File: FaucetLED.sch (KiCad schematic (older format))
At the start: 25 parts, among them P1 CONN_01X13, P2 CONN_01X02, U1 MAX4256

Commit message: WIP version 2 with STM32L0.
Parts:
- removed D1: LED_RCBG, Pin_Headers:Pin_Header_Straight_1x04, symbol LED_RCBG
- removed P1: CONN_01X13, Socket_Strips:Socket_Strip_Straight_1x13, symbol CONN_01X13
- removed P2: CONN_01X02, Pin_Headers:Pin_Header_Straight_1x02, symbol CONN_01X02
- removed R10: 68R, Resistors_ThroughHole:Resistor_Horizontal_RM10mm, symbol R
- removed R11, R12: 10R, Resistors_ThroughHole:Resistor_Horizontal_RM10mm, symbol R
- removed R3, R5: 100M, Resistors_ThroughHole:Resistor_Horizontal_RM10mm, symbol R
- removed R6: 680R, Resistors_ThroughHole:Resistor_Horizontal_RM10mm, symbol R
- removed TH1: THERMISTOR, Pin_Headers:Pin_Header_Straight_1x02, symbol THERMISTOR
- removed U1: MAX4256, Housings_SOIC:SOIC-8_3.9x4.9mm_Pitch1.27mm, symbol MAX4256
- added BT2: LiIon, Pin_Headers:Pin_Header_Angled_1x02_Pitch2.00mm, symbol Battery
- added C3: 0.1u, Capacitors_SMD:C_0603, symbol C
- added D1: LED, LEDs:LED_0805, symbol LED
- added L1: Bead, Resistors_SMD:R_0603, symbol L_Small
- added P1: CONN_01X07, Pin_Headers:Pin_Header_Straight_1x07_Pitch2.54mm, symbol CONN_01X07
- added P2: CONN_01X03, Pin_Headers:Pin_Header_Straight_1x03_Pitch2.54mm, symbol CONN_01X03
- added R1: 100R, Resistors_SMD:R_0603, symbol R
- added R4: 10k, Resistors_SMD:R_0603, symbol R
- added R9: 1k, Resistors_SMD:R_0603, symbol R
- added U1: TLV70033DDC, TO_SOT_Packages_SMD:SOT-23-5, symbol TLV70033DDC
- added U2: STM32L052KxTx, Housings_QFP:LQFP-32_7x7mm_Pitch0.8mm, symbol STM32L052KxTx
- added W1: TEST_1P, Measurement_Points:Measurement_Point_Round-SMD-Pad_Small, symbol TEST_1P
- BT1: value Battery -> CR2016x2; footprint Pin_Headers:Pin_Header_Straight_1x02 -> Connect:CR2032H
- C1: value 10n -> 0.1u; footprint Capacitors_ThroughHole:C_Rect_L7_W2_P5 -> Capacitors_SMD:C_0603
- C2: value 10p -> 1u; footprint Capacitors_ThroughHole:C_Rect_L7_W2_P5 -> Capacitors_SMD:C_0603
- C4: value 10p -> 0.47u; footprint Capacitors_ThroughHole:C_Rect_L7_W2_P5 -> Capacitors_SMD:C_0603
- C6: value 0.1u -> 1u; footprint Capacitors_ThroughHole:C_Rect_L7_W2_P5 -> Capacitors_SMD:C_0603
- C7: renamed from C3; value 1u -> 0.1u; footprint Capacitors_ThroughHole:C_Rect_L7_W2_P5 -> Capacitors_SMD:C_0603
- C8: renamed from C5; footprint Capacitors_ThroughHole:C_Rect_L7_W2_P5 -> Capacitors_SMD:C_0603
- C9: renamed from C7; footprint Capacitors_ThroughHole:C_Rect_L7_W2_P5 -> Capacitors_SMD:C_0603
- R2: renamed from R1; footprint Resistors_ThroughHole:Resistor_Horizontal_RM10mm -> Resistors_SMD:R_0603
- R3: renamed from R2; footprint Resistors_ThroughHole:Resistor_Horizontal_RM10mm -> Resistors_SMD:R_0603
- R5: renamed from R4; footprint Resistors_ThroughHole:Resistor_Horizontal_RM10mm -> Resistors_SMD:R_0603
- R6: renamed from R7; value 68R -> 78R; footprint Resistors_ThroughHole:Resistor_Horizontal_RM10mm -> Resistors_SMD:R_0603
- R7: renamed from R8; value 15R -> 12R; footprint Resistors_ThroughHole:Resistor_Horizontal_RM10mm -> Resistors_SMD:R_0603
- R8: renamed from R9; value 15R -> 25R; footprint Resistors_ThroughHole:Resistor_Horizontal_RM10mm -> Resistors_SMD:R_0603
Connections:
- net labels added: BATT_2, LED_B_OUT, LED_DBG, LED_G_OUT, LED_R_OUT, MCO, RESET, SWCLK, SWDIO, THERM_SENSE, THERM_SW, TSC_IN, TSC_SAMPLING
- net labels removed: AMP_SHDN, PIEZO_1, PIEZO_2, PIEZO_AMP, THERM_1, THERM_2, T_SENSE, VCC_2, VCC_2_BUF
- wire segments 84 -> 79
- no-connect marks 4 -> 13
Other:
- moved on the sheet: BT1, C7, C8, C9, R2, R3, R5, R6, R7, R8

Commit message: Add battery holder, more connectors.
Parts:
- removed P1: CONN_01X07, Pin_Headers:Pin_Header_Straight_1x07_Pitch2.54mm, symbol CONN_01X07
- added D1: D_Schottky_x2_KCom_AAK, TO_SOT_Packages_SMD:SOT-23, symbol D_Schottky_x2_KCom_AAK
- added P1: CONN_01X03, Pin_Headers:Pin_Header_Straight_1x03_Pitch2.54mm, symbol CONN_01X03
- added P2, P3, P5: CONN_01X02, Pin_Headers:Pin_Header_Straight_2x01_Pitch2.54mm, symbol CONN_01X02
- BT1: footprint Connect:CR2032H -> components:Keystone_3020_CR2016x2
- U1: DigiKey PN (none) -> 296-27937-1-ND
- renumbered C6 to C5, C7 to C6, C8 to C7, C9 to C8, D1 to D2, P2 to P4
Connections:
- wire segments 79 -> 86
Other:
- moved on the sheet: BT1, C1, C2, C5, P4, U1

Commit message: Add part numbers for more parts.
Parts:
- BT1: DigiKey PN (none) -> 36-3020-ND; Manufacturer PN (none) -> 3020
- D2: DigiKey PN (none) -> 67-2191-1-ND
- L1: Manufacturer PN (none) -> BK1608HW601-T
- U1: Manufacturer PN (none) -> TLV70033DDCR
- U2: DigiKey PN (none) -> 497-14904-ND; Manufacturer PN (none) -> STM32L052K8T6
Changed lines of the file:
@@
 F 2 "components:Keystone_3020_CR2016x2" V 1400 1440 50  0001 C CNN
 F 3 "" V 1400 1440 50  0000 C CNN
+F 4 "36-3020-ND" H 1400 1400 60  0001 C CNN "DigiKey PN"
+F 5 "3020" H 1400 1400 60  0001 C CNN "Manufacturer PN"
 	1    1400 1400
 	1    0    0    -1
@@
 F 2 "Housings_QFP:LQFP-32_7x7mm_Pitch0.8mm" H 5500 2250 60  0001 C CNN
 F 3 "" H 5500 2250 60  0001 C CNN
+F 4 "497-14904-ND" H 5600 3100 60  0001 C CNN "DigiKey PN"
+F 5 "STM32L052K8T6" H 5600 3100 60  0001 C CNN "Manufacturer PN"
 	1    5600 3100
 	1    0    0    -1
@@
 F 3 "" H 4500 1150 50  0000 C CNN
 F 4 "296-27937-1-ND" H 4500 1150 60  0001 C CNN "DigiKey PN"
+F 5 "TLV70033DDCR" H 4500 1150 60  0001 C CNN "Manufacturer PN"
 	1    4500 1150
 	1    0    0    -1
@@
 F 2 "LEDs:LED_0805" H 8850 3250 50  0001 C CNN
 F 3 "" H 8850 3250 50  0000 C CNN
+F 4 "67-2191-1-ND" H 8850 3250 60  0001 C CNN "DigiKey PN"
 	1    8850 3250
 	-1   0    0    1
@@
 F 3 "" H 5800 2050 50  0000 C CNN
 F 4 "587-1879-1-ND" H 5800 2050 60  0001 C CNN "DigiKey PN"
+F 5 "BK1608HW601-T" H 5800 2050 60  0001 C CNN "Manufacturer PN"
 	1    5800 2050
 	1    0    0    -1

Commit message: Update R and C footprints for 0603/0805 compatibility.
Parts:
- C1, C2, C3, C4, C5, C6, C7, C8: footprint Capacitors_SMD:C_0603 -> components:C_0603_0805
- R1, R2, R3, R4, R5, R6, R7, R8, R9: footprint Resistors_SMD:R_0603 -> components:R_0603_0805
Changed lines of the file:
@@
 F 0 "R5" V 5480 5950 50  0000 C CNN
 F 1 "10k" V 5400 5950 50  0000 C CNN
-F 2 "Resistors_SMD:R_0603" V 5330 5950 50  0001 C CNN
+F 2 "components:R_0603_0805" V 5330 5950 50  0001 C CNN
 F 3 "" H 5400 5950 50  0000 C CNN
 	1    5400 5950
@@
 F 0 "R2" V 4030 5950 50  0000 C CNN
 F 1 "1M" V 3950 5950 50  0000 C CNN
-F 2 "Resistors_SMD:R_0603" V 3880 5950 50  0001 C CNN
+F 2 "components:R_0603_0805" V 3880 5950 50  0001 C CNN
 F 3 "" H 3950 5950 50  0000 C CNN
 	1    3950 5950
@@
 F 0 "R3" V 4030 6450 50  0000 C CNN
 F 1 "1M" V 3950 6450 50  0000 C CNN
-F 2 "Resistors_SMD:R_0603" V 3880 6450 50  0001 C CNN
+F 2 "components:R_0603_0805" V 3880 6450 50  0001 C CNN
 F 3 "" H 3950 6450 50  0000 C CNN
 	1    3950 6450
@@
 F 0 "C7" H 6375 1700 50  0000 L CNN
 F 1 "0.1u" H 6375 1500 50  0000 L CNN
-F 2 "Capacitors_SMD:C_0603" H 6388 1450 50  0001 C CNN
+F 2 "components:C_0603_0805" H 6388 1450 50  0001 C CNN
 F 3 "" H 6350 1600 50  0000 C CNN
 	1    6350 1600
@@
 F 0 "C8" H 6775 1700 50  0000 L CNN
 F 1 "1u" H 6775 1500 50  0000 L CNN
-F 2 "Capacitors_SMD:C_0603" H 6788 1450 50  0001 C CNN
+F 2 "components:C_0603_0805" H 6788 1450 50  0001 C CNN
 F 3 "" H 6750 1600 50  0000 C CNN
 	1    6750 1600
@@
 F 0 "C6" H 5425 6550 50  0000 L CNN
 F 1 "0.1u" H 5425 6350 50  0000 L CNN
-F 2 "Capacitors_SMD:C_0603" H 5438 6300 50  0001 C CNN
+F 2 "components:C_0603_0805" H 5438 6300 50  0001 C CNN
 F 3 "" H 5400 6450 50  0000 C CNN
 	1    5400 6450
@@
 F 0 "R7" V 8480 4700 50  0000 C CNN
 F 1 "12R" V 8400 4700 50  0000 C CNN
-F 2 "Resistors_SMD:R_0603" V 8330 4700 50  0001 C CNN
+F 2 "components:R_0603_0805" V 8330 4700 50  0001 C CNN
 F 3 "" H 8400 4700 50  0000 C CNN
 	1    8400 4700
@@
 F 0 "R8" V 8480 4900 50  0000 C CNN
 F 1 "25R" V 8400 4900 50  0000 C CNN
-F 2 "Resistors_SMD:R_0603" V 8330 4900 50  0001 C CNN
+F 2 "components:R_0603_0805" V 8330 4900 50  0001 C CNN
 F 3 "" H 8400 4900 50  0000 C CNN
 	1    8400 4900
@@
 F 0 "R6" V 8480 4500 50  0000 C CNN
 F 1 "78R" V 8400 4500 50  0000 C CNN
-F 2 "Resistors_SMD:R_0603" V 8330 4500 50  0001 C CNN
+F 2 "components:R_0603_0805" V 8330 4500 50  0001 C CNN
 F 3 "" H 8400 4500 50  0000 C CNN
 	1    8400 4500
@@
 F 0 "C4" H 4075 4300 50  0000 L CNN
 F 1 "0.47u" H 4075 4100 50  0000 L CNN
-F 2 "Capacitors_SMD:C_0603" H 4088 4050 50  0001 C CNN
+F 2 "components:C_0603_0805" H 4088 4050 50  0001 C CNN
 F 3 "" H 4050 4200 50  0000 C CNN
 	1    4050 4200
@@
 F 0 "R4" V 4630 3150 50  0000 C CNN
 F 1 "10k" V 4550 3150 50  0000 C CNN
-F 2 "Resistors_SMD:R_0603" V 4480 3150 50  0001 C CNN
+F 2 "components:R_0603_0805" V 4480 3150 50  0001 C CNN
 F 3 "" H 4550 3150 50  0000 C CNN
 	1    4550 3150
@@
 F 0 "C3" H 3975 3200 50  0000 L CNN
 F 1 "0.1u" H 3975 3000 50  0000 L CNN
-F 2 "Capacitors_SMD:C_0603" H 3988 2950 50  0001 C CNN
+F 2 "components:C_0603_0805" H 3988 2950 50  0001 C CNN
 F 3 "" H 3950 3100 50  0000 C CNN
 	1    3950 3100
@@
 F 0 "C5" H 5225 1400 50  0000 L CNN
 F 1 "1u" H 5225 1200 50  0000 L CNN
-F 2 "Capacitors_SMD:C_0603" H 5238 1150 50  0001 C CNN
+F 2 "components:C_0603_0805" H 5238 1150 50  0001 C CNN
 F 3 "" H 5200 1300 50  0000 C CNN
 	1    5200 1300
@@
 F 0 "C2" H 3775 1400 50  0000 L CNN
 F 1 "1u" H 3775 1200 50  0000 L CNN
-F 2 "Capacitors_SMD:C_0603" H 3788 1150 50  0001 C CNN
+F 2 "components:C_0603_0805" H 3788 1150 50  0001 C CNN
 F 3 "" H 3750 1300 50  0000 C CNN
 	1    3750 1300
@@
 F 0 "C1" H 3525 1400 50  0000 L CNN
 F 1 "0.1u" H 3525 1200 50  0000 L CNN
-F 2 "Capacitors_SMD:C_0603" H 3538 1150 50  0001 C CNN
+F 2 "components:C_0603_0805" H 3538 1150 50  0001 C CNN
 F 3 "" H 3500 1300 50  0000 C CNN
 	1    3500 1300
@@
 F 0 "R9" V 8530 3250 50  0000 C CNN
 F 1 "1k" V 8450 3250 50  0000 C CNN
-F 2 "Resistors_SMD:R_0603" V 8380 3250 50  0001 C CNN
+F 2 "components:R_0603_0805" V 8380 3250 50  0001 C CNN
 F 3 "" H 8450 3250 50  0000 C CNN
 	1    8450 3250
@@
 F 0 "R1" V 3830 4000 50  0000 C CNN
 F 1 "100R" V 3750 4000 50  0000 C CNN
-F 2 "Resistors_SMD:R_0603" V 3680 4000 50  0001 C CNN
+F 2 "components:R_0603_0805" V 3680 4000 50  0001 C CNN
 F 3 "" H 3750 4000 50  0000 C CNN
 	1    3750 4000

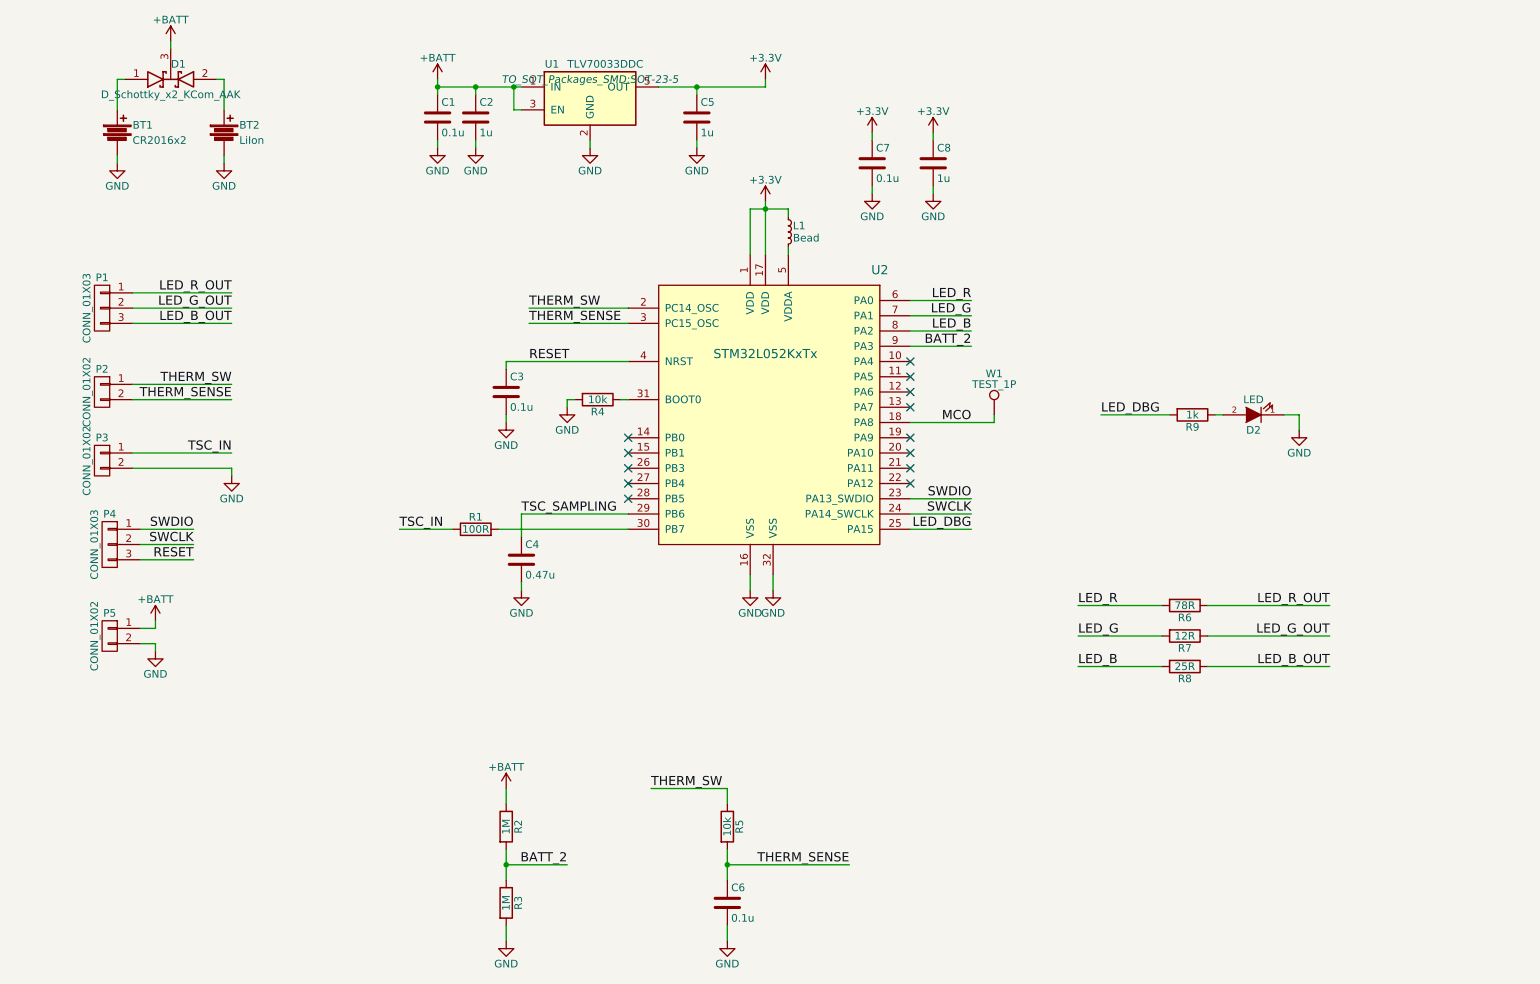
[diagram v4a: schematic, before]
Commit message: Add 5V regulator, LED drive NMOS. Not layed out in PCB yet.
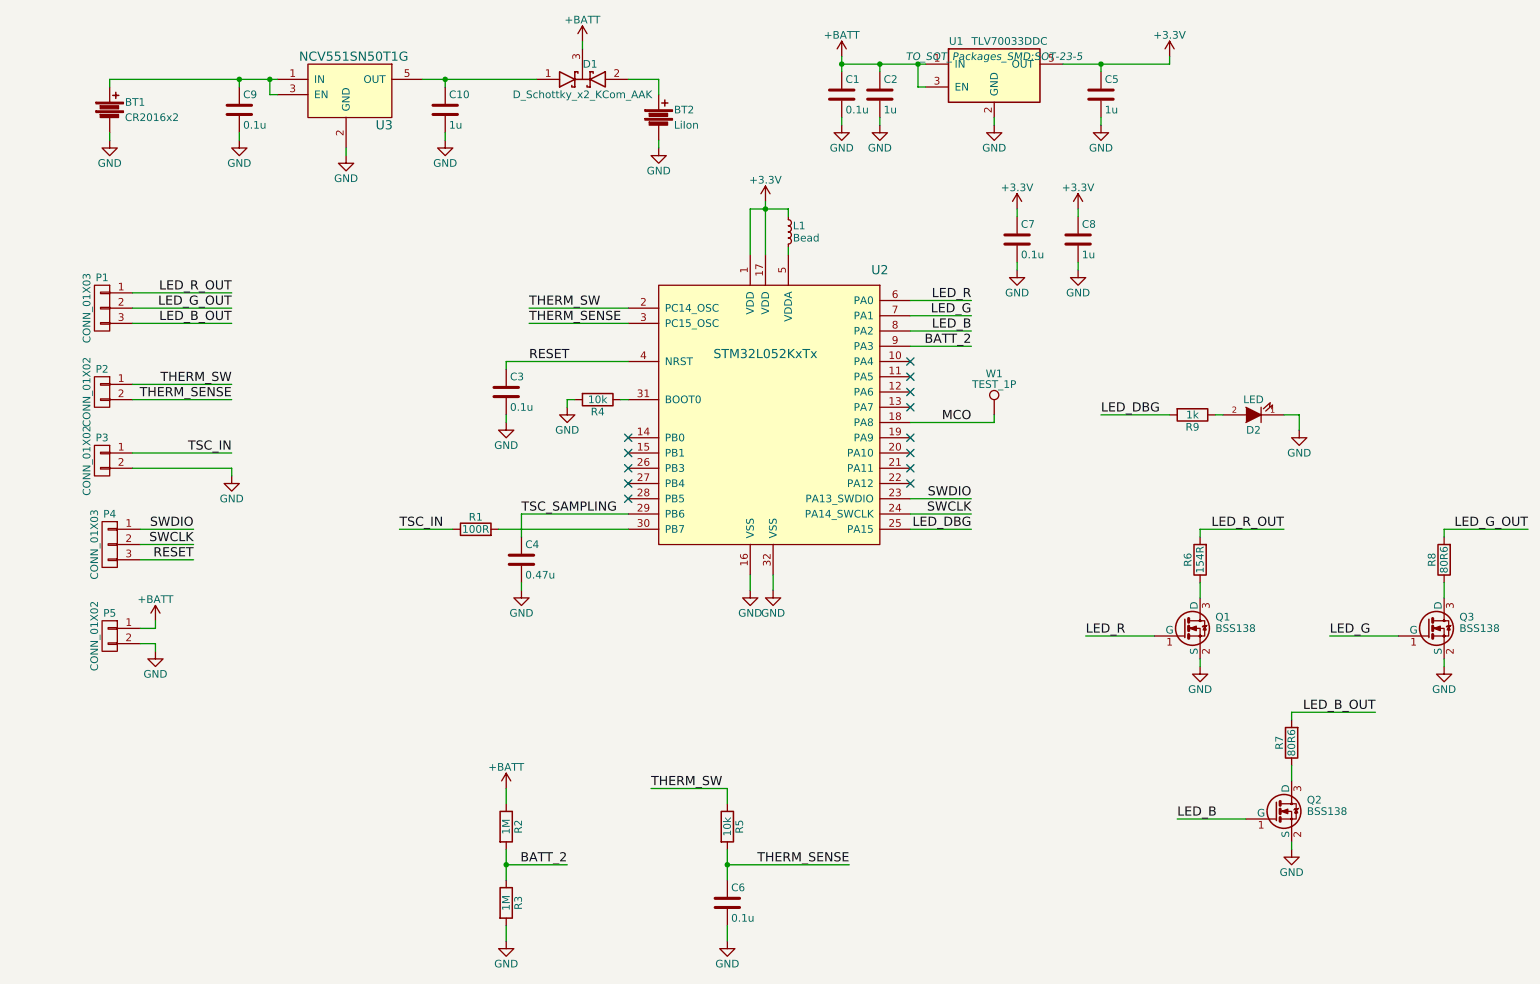
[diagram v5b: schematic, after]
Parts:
- added C10: 1u, components:C_0603_0805, symbol C
- added C9: 0.1u, components:C_0603_0805, symbol C
- added Q1, Q2, Q3: BSS138, TO_SOT_Packages_SMD:SOT-23, symbol BSS138
- added U3: NCV551SN50T1G, TO_SOT_Packages_SMD:SOT-23-5, symbol NCV551SN50T1G
- R6: value 78R -> 154R
- R7: value 12R -> 80R6
- R8: value 25R -> 80R6
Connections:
- net GND: now also C10.2, C9.2, Q1.2 (S), Q2.2 (S), Q3.2 (S), U3.2 (GND)
- net LED_B: now also Q2.1 (G); no longer R8.2
- net LED_B_OUT: now also R7.2; no longer R8.1
- net LED_G: now also Q3.1 (G); no longer R7.2
- net LED_G_OUT: now also R8.2; no longer R7.1
- net LED_R: now also Q1.1 (G); no longer R6.2
- net LED_R_OUT: now also R6.2; no longer R6.1
- net at BT1.1: now also C9.1, U3.1 (IN), U3.3 (EN); no longer D1.1 (A)
- new net: Q1.3 (D), R6.1
- new net: C10.1, D1.1 (A), U3.5 (OUT)
- new net: Q3.3 (D), R8.1
- new net: Q2.3 (D), R7.1
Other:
- moved on the sheet: BT1, BT2, C1, C2, C5, C7, C8, D1, R6, U1

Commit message: More schematic tweaks to resistor values.
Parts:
- removed C2: 1u, components:C_0603_0805, symbol C
- removed P5: CONN_01X02, Pin_Headers:Pin_Header_Straight_2x01_Pitch2.54mm, symbol CONN_01X02
- P1, P4: footprint Pin_Headers:Pin_Header_Straight_1x03_Pitch2.54mm -> Pin_Headers:Pin_Header_Straight_1x04_Pitch2.54mm; symbol CONN_01X03 -> CONN_01X04
- P2: footprint Pin_Headers:Pin_Header_Straight_2x01_Pitch2.54mm -> Pin_Headers:Pin_Header_Straight_1x02_Pitch2.54mm
- P3: footprint Pin_Headers:Pin_Header_Straight_2x01_Pitch2.54mm -> Pin_Headers:Pin_Header_Straight_1x01_Pitch2.54mm; symbol CONN_01X02 -> CONN_01X01
- R6: value 154R -> 130R; DigiKey PN (none) -> 311-130HRCT-ND
- U3: symbol NCV551SN50T1G -> NCV551SN50T1G-RESCUE-FaucetLED
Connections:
- net +BATT: now also P1.1 (P1)
- net GND: now also P4.4 (P4); no longer P3.2 (P2)
- net LED_B_OUT renamed LED_B_CONN
- net LED_B_CONN: now also P1.4 (P4); no longer P1.3 (P3)
- net LED_G_OUT renamed LED_G_CONN
- net LED_G_CONN: now also P1.3 (P3); no longer P1.2 (P2)
- net LED_R_OUT renamed LED_R_CONN
- net LED_R_CONN: now also P1.2 (P2); no longer P1.1 (P1)
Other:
- moved on the sheet: C1, C7, C8, D2, R9
